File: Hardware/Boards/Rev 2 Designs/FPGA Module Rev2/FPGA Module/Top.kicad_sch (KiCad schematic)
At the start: 6 parts

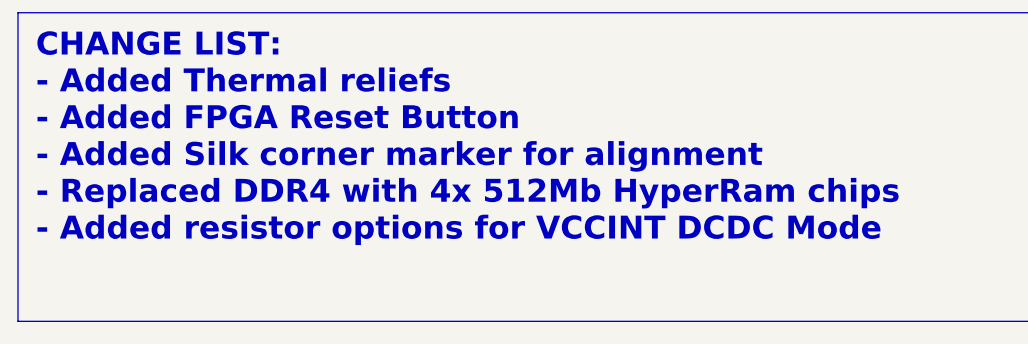
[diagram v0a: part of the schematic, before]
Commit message: Rev 2 IO module complete
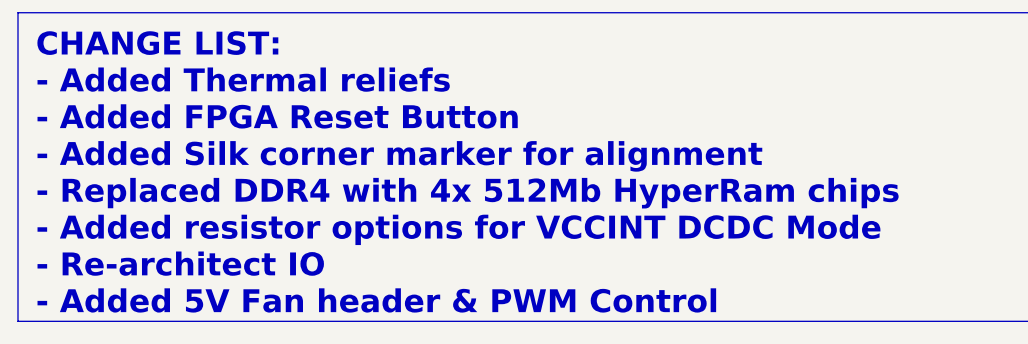
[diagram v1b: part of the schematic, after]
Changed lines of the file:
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@@
 		)
 	)
-	(text_box "CHANGE LIST:\n- Added Thermal reliefs\n- Added FPGA Reset Button\n- Added Silk corner marker for alignment\n- Replaced DDR4 with 4x 512Mb HyperRam chips\n- Added resistor options for VCCINT DCDC Mode\n"
+	(text_box "CHANGE LIST:\n- Added Thermal reliefs\n- Added FPGA Reset Button\n- Added Silk corner marker for alignment\n- Replaced DDR4 with 4x 512Mb HyperRam chips\n- Added resistor options for VCCINT DCDC Mode\n- Re-architect IO\n- Added 5V Fan header & PWM Control\n"
 		(exclude_from_sim no)
 		(at 17.78 247.015 0)

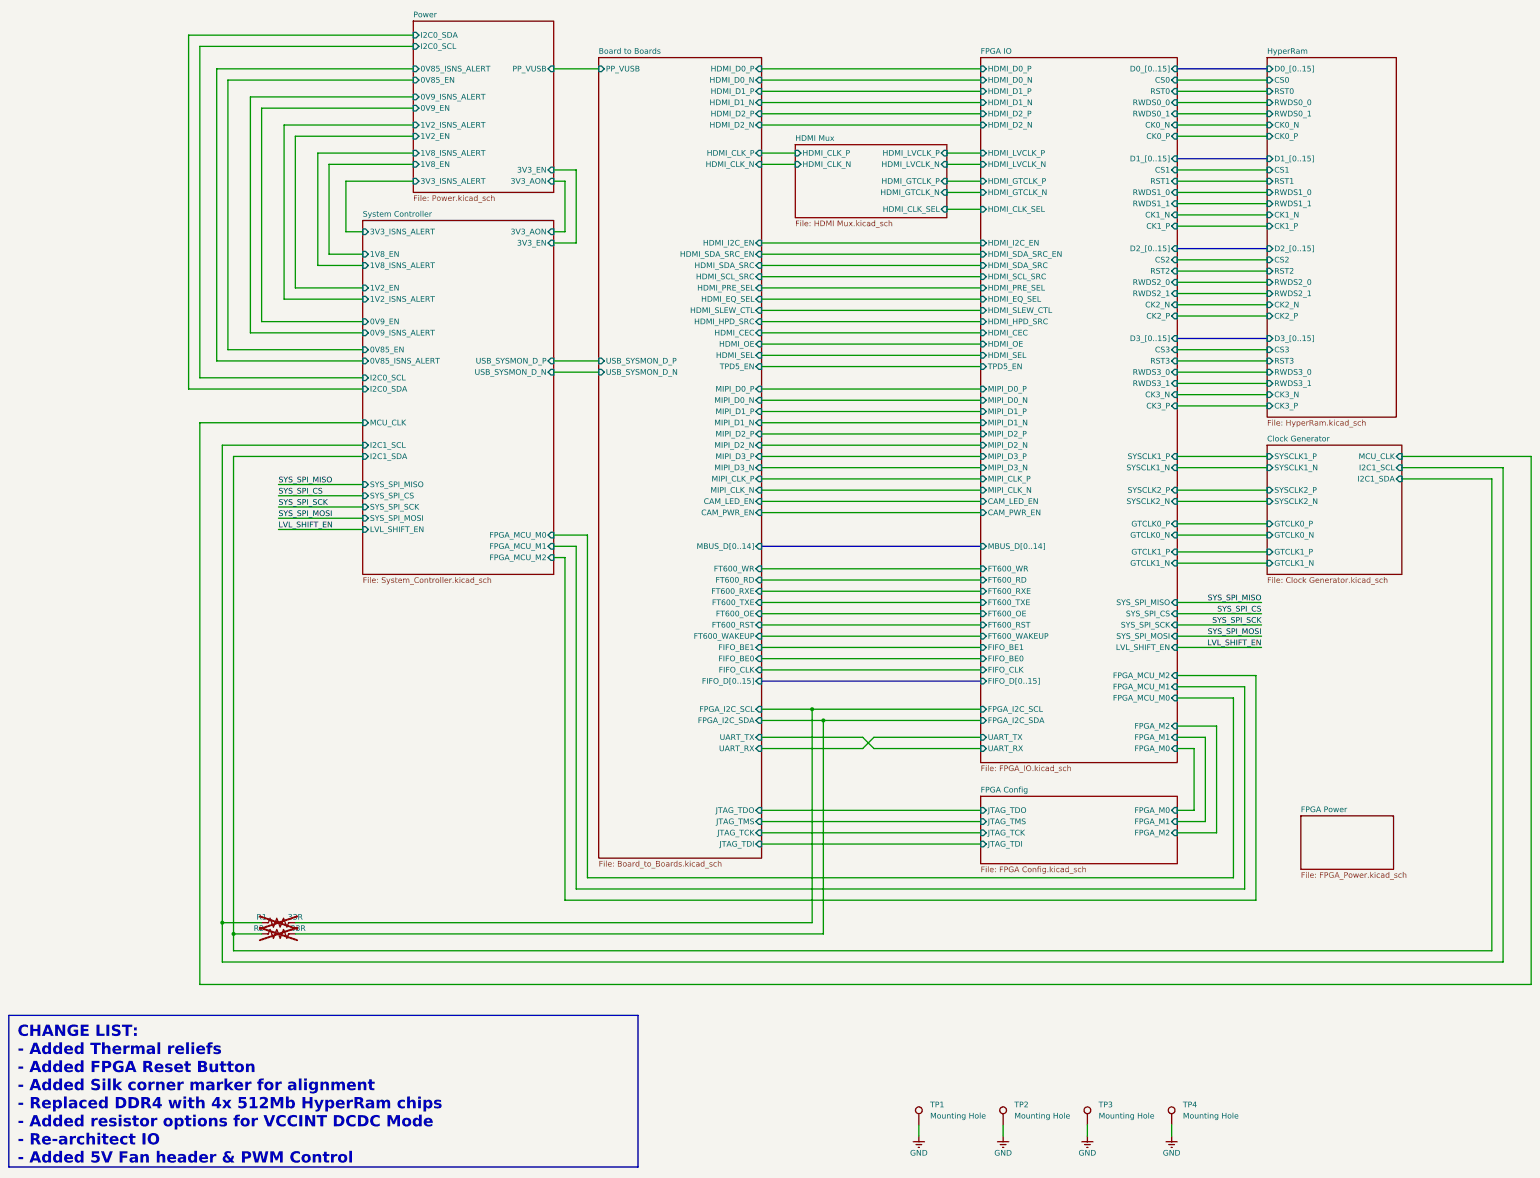
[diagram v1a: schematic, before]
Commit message: FPGA Module Rev 2 Layout Begun
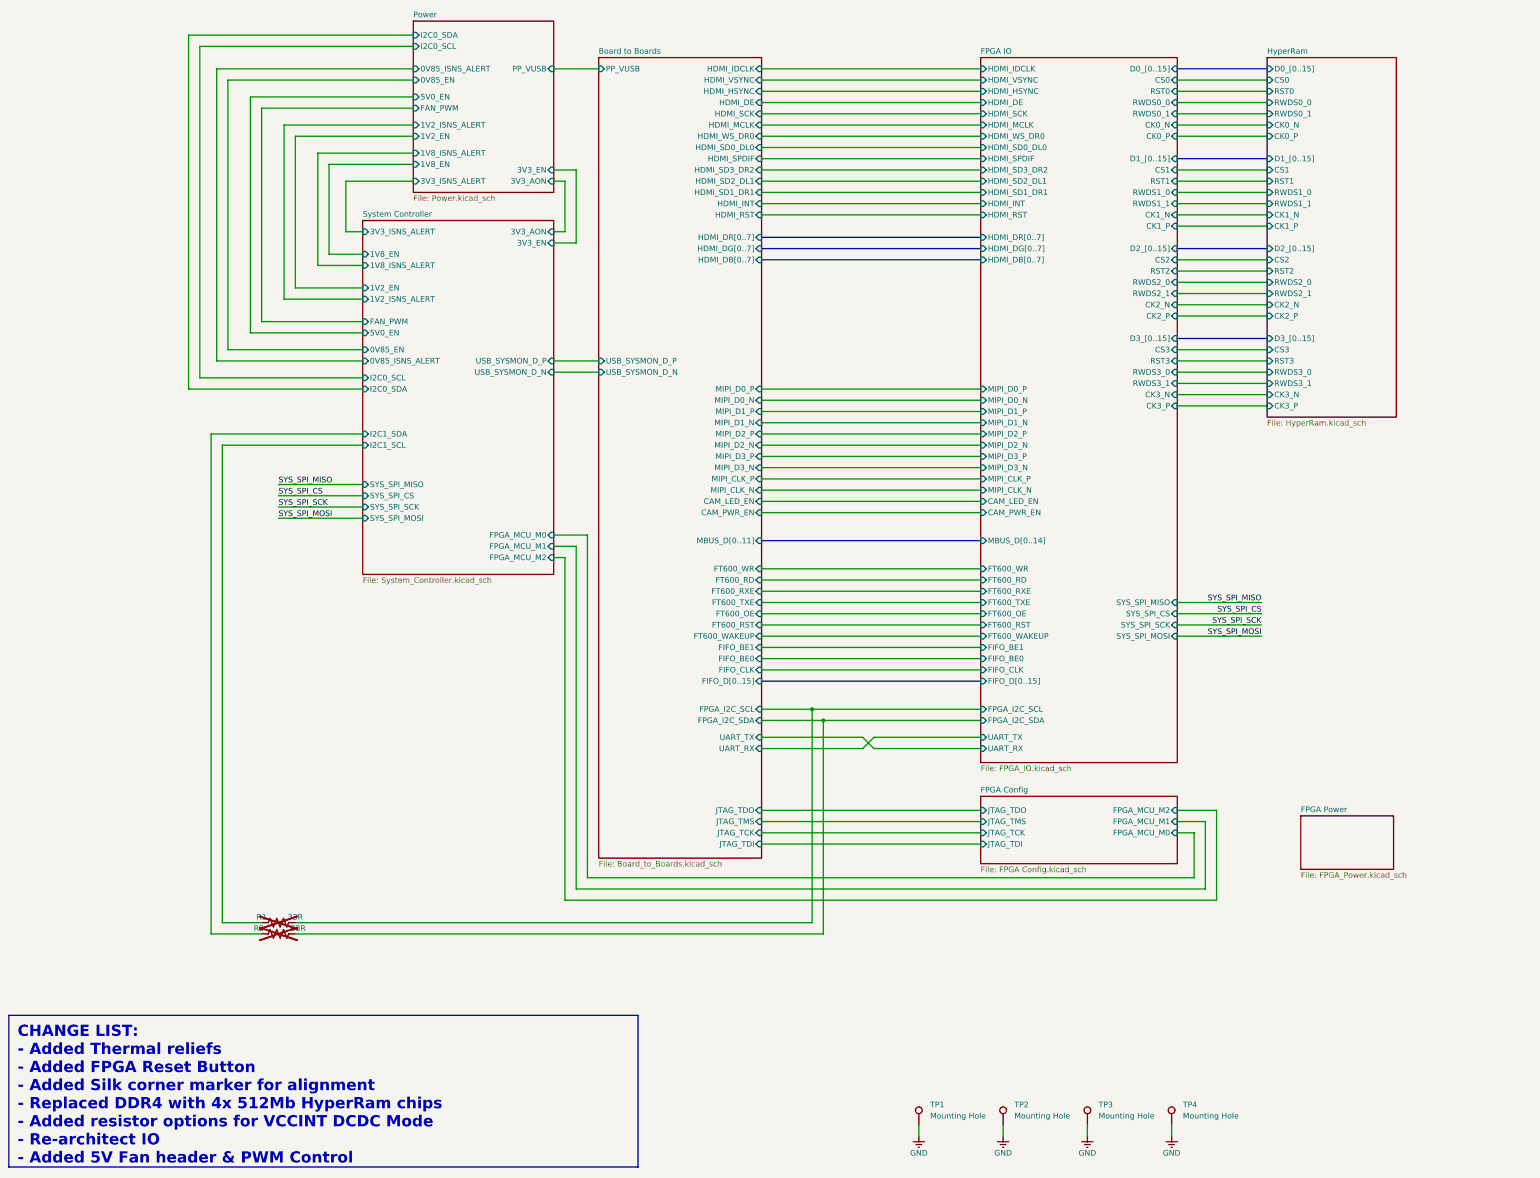
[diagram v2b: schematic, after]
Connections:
- net Clock Generator/I2C1_SCL renamed System Controller/I2C1_SCL
- net Clock Generator/I2C1_SDA renamed System Controller/I2C1_SDA
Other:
- removed sheet Clock Generator
- removed sheet HDMI Mux
- sheet Board to Boards ports: added HDMI_DB[0..7], HDMI_DE, HDMI_DG[0..7], HDMI_DR[0..7], HDMI_HSYNC, HDMI_IDCLK, HDMI_INT, HDMI_MCLK, HDMI_RST, HDMI_SCK, HDMI_SD0_DL0, HDMI_SD1_DR1, HDMI_SD2_DL1, HDMI_SD3_DR2, HDMI_SPDIF, HDMI_VSYNC, HDMI_WS_DR0, MBUS_D[0..11]; removed HDMI_CEC, HDMI_CLK_N, HDMI_CLK_P, HDMI_D0_N, HDMI_D0_P, HDMI_D1_N, HDMI_D1_P, HDMI_D2_N, HDMI_D2_P, HDMI_EQ_SEL, HDMI_HPD_SRC, HDMI_I2C_EN, HDMI_OE, HDMI_PRE_SEL, HDMI_SCL_SRC, HDMI_SDA_SRC, HDMI_SDA_SRC_EN, HDMI_SEL, HDMI_SLEW_CTL, MBUS_D[0..14], TPD5_EN
- sheet FPGA Config ports: added FPGA_MCU_M0, FPGA_MCU_M1, FPGA_MCU_M2; removed FPGA_M0, FPGA_M1, FPGA_M2
- sheet FPGA IO ports: added HDMI_DB[0..7], HDMI_DE, HDMI_DG[0..7], HDMI_DR[0..7], HDMI_HSYNC, HDMI_IDCLK, HDMI_INT, HDMI_MCLK, HDMI_RST, HDMI_SCK, HDMI_SD0_DL0, HDMI_SD1_DR1, HDMI_SD2_DL1, HDMI_SD3_DR2, HDMI_SPDIF, HDMI_VSYNC, HDMI_WS_DR0; removed FPGA_M0, FPGA_M1, FPGA_M2, FPGA_MCU_M0, FPGA_MCU_M1, FPGA_MCU_M2, GTCLK0_N, GTCLK0_P, GTCLK1_N, GTCLK1_P, HDMI_CEC, HDMI_CLK_SEL, HDMI_D0_N, HDMI_D0_P, HDMI_D1_N, HDMI_D1_P, HDMI_D2_N, HDMI_D2_P, HDMI_EQ_SEL, HDMI_GTCLK_N, HDMI_GTCLK_P, HDMI_HPD_SRC, HDMI_I2C_EN, HDMI_LVCLK_N, HDMI_LVCLK_P, HDMI_OE, HDMI_PRE_SEL, HDMI_SCL_SRC, HDMI_SDA_SRC, HDMI_SDA_SRC_EN, HDMI_SEL, HDMI_SLEW_CTL, LVL_SHIFT_EN, SYSCLK1_N, SYSCLK1_P, SYSCLK2_N, SYSCLK2_P, TPD5_EN
- sheet Power ports: added 5V0_EN, FAN_PWM; removed 0V9_EN, 0V9_ISNS_ALERT
- sheet System Controller ports: added 5V0_EN, FAN_PWM; removed 0V9_EN, 0V9_ISNS_ALERT, LVL_SHIFT_EN, MCU_CLK

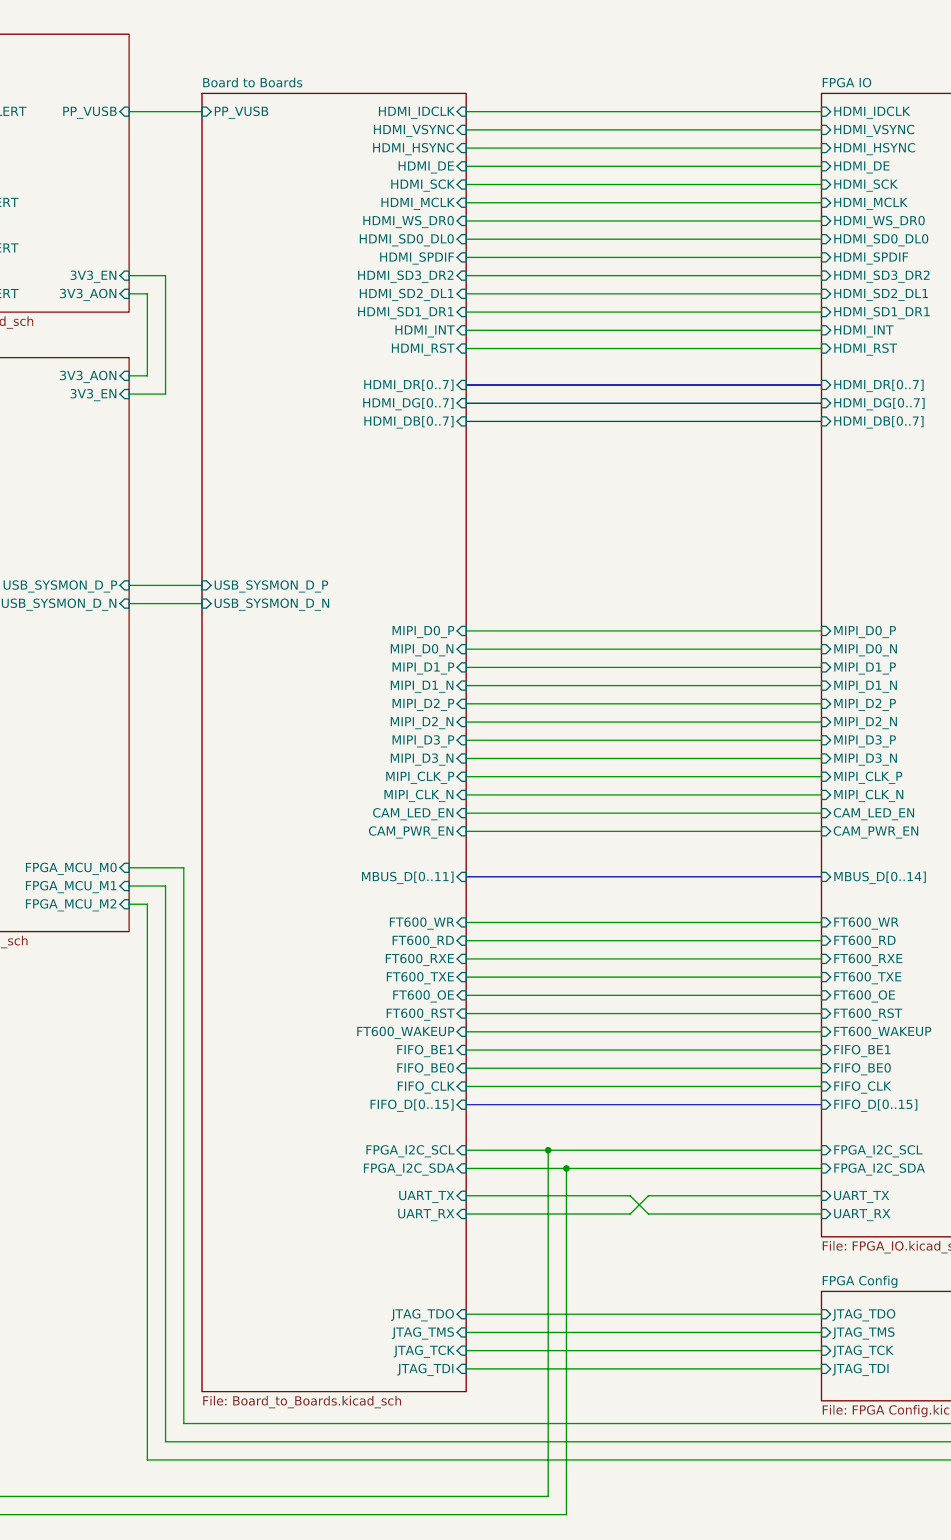
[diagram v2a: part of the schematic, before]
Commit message: Updated Schematics & created pixel combiner HDL
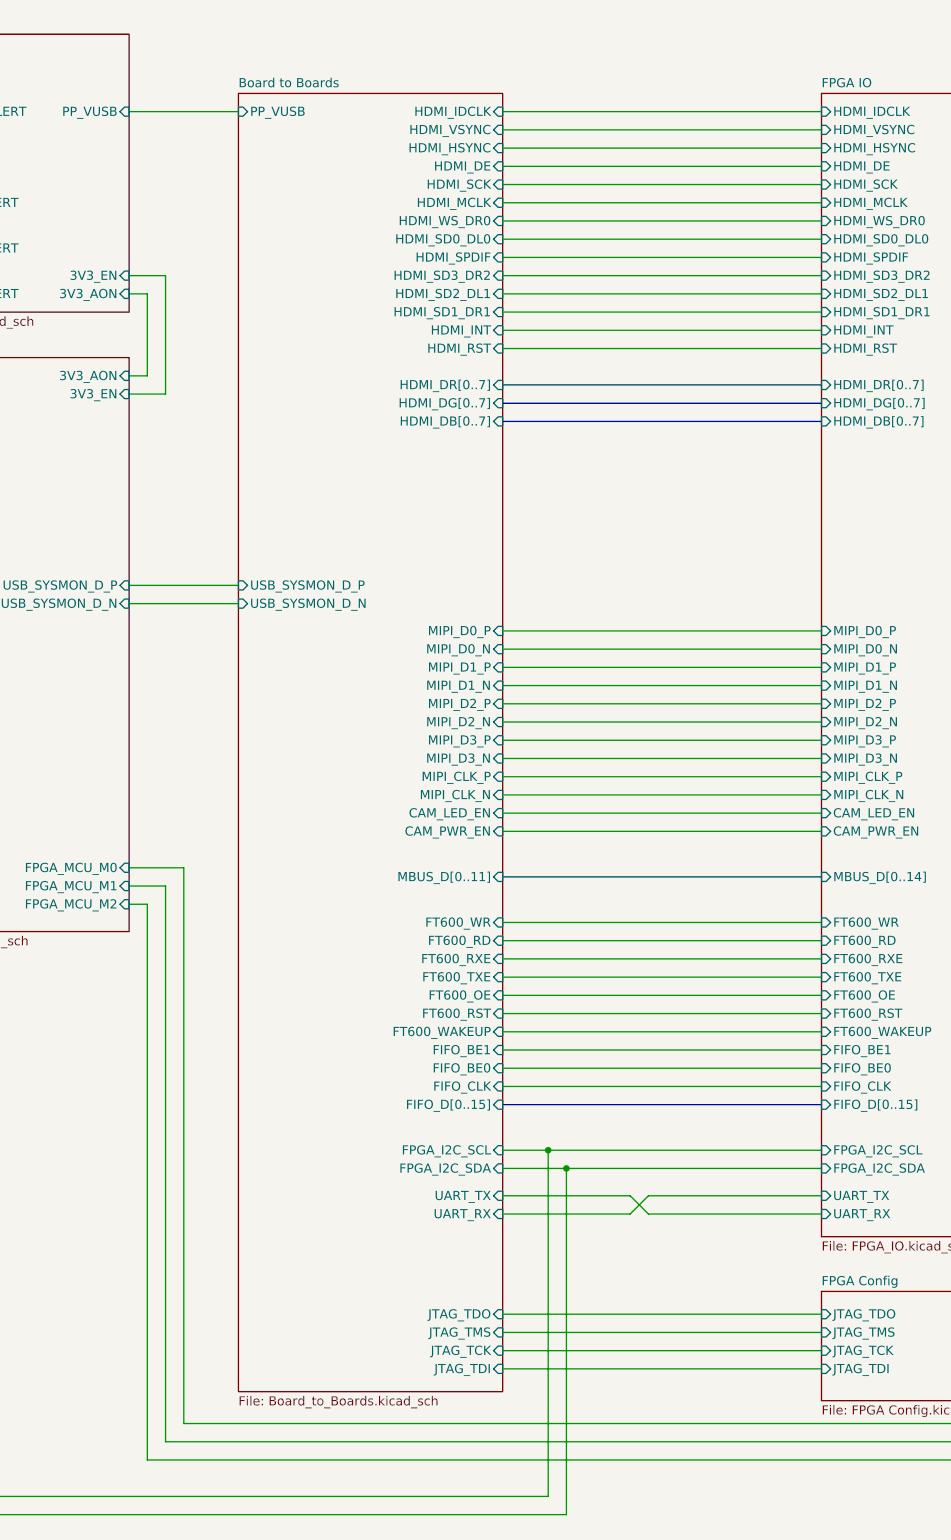
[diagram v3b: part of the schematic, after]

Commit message: Added diagrams, papers and presentations
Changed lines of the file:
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@@
 (kicad_sch
-	(version 20231120)
+	(version 20250114)
 	(generator "eeschema")
-	(generator_version "8.0")
+	(generator_version "9.0")
 	(paper "A3")
 	(title_block
@@
 		(comment 1 "Designed by John Hofmeyr")
 	)
+	(text_box "CHANGE LIST:\n- Added Thermal reliefs\n- Added FPGA Reset Button\n- Added Silk corner marker for alignment\n- Replaced DDR4 with 4x 512Mb HyperRam chips\n- Added resistor options for VCCINT DCDC Mode\n- Re-architect IO\n- Added 5V Fan header & PWM Control\n"
+		(exclude_from_sim no)
+		(at 17.78 247.015 0)
+		(size 142.24 34.29)
+		(margins 1.905 1.905 1.905 1.905)
+		(stroke
+			(width 0)
+			(type default)
+		)
+		(fill
+			(type none)
+		)
+		(effects
+			(font
+				(size 2.54 2.54)
+				(thickness 0.508)
+				(bold yes)
+			)
+			(justify left top)
+		)
+	)
 	(junction
 		(at 201.93 180.34)
@@
 		)
 	)
-	(text_box "CHANGE LIST:\n- Added Thermal reliefs\n- Added FPGA Reset Button\n- Added Silk corner marker for alignment\n- Replaced DDR4 with 4x 512Mb HyperRam chips\n- Added resistor options for VCCINT DCDC Mode\n- Re-architect IO\n- Added 5V Fan header & PWM Control\n"
-		(exclude_from_sim no)
-		(at 17.78 247.015 0)
-		(size 142.24 34.29)
-		(stroke
-			(width 0)
-			(type default)
-		)
-		(fill
-			(type none)
-		)
-		(effects
-			(font
-				(size 2.54 2.54)
-				(thickness 0.508)
-				(bold yes)
-			)
-			(justify left top)
-		)
-	)
 	(label "SYS_SPI_MOSI"
 		(at 78.74 134.62 0)
-		(fields_autoplaced yes)
 		(effects
 			(font
@@
 	(label "SYS_SPI_MISO"
 		(at 78.74 127 0)
-		(fields_autoplaced yes)
 		(effects
 			(font
@@
 	(label "SYS_SPI_MOSI"
 		(at 300.99 161.29 180)
-		(fields_autoplaced yes)
 		(effects
 			(font
@@
 	(label "SYS_SPI_CS"
 		(at 78.74 129.54 0)
-		(fields_autoplaced yes)
 		(effects
 			(font
@@
 	(label "SYS_SPI_SCK"
 		(at 78.74 132.08 0)
-		(fields_autoplaced yes)
 		(effects
 			(font
@@
 	(label "SYS_SPI_MISO"
 		(at 300.99 153.67 180)
-		(fields_autoplaced yes)
 		(effects
 			(font
@@
 	(label "SYS_SPI_CS"
 		(at 300.99 156.21 180)
-		(fields_autoplaced yes)
 		(effects
 			(font
@@
 	(label "SYS_SPI_SCK"
 		(at 300.99 158.75 180)
-		(fields_autoplaced yes)
 		(effects
 			(font
@@
 		(at 237.49 197.485)
 		(size 44.45 15.24)
+		(exclude_from_sim no)
+		(in_bom yes)
+		(on_board yes)
+		(dnp no)
 		(fields_autoplaced yes)
 		(stroke
@@
 		(at 109.22 22.225)
 		(size 31.75 38.735)
+		(exclude_from_sim no)
+		(in_bom yes)
+		(on_board yes)
+		(dnp no)
 		(fields_autoplaced yes)
 		(stroke
@@
 		(at 302.26 30.48)
 		(size 29.21 81.28)
+		(exclude_from_sim no)
+		(in_bom yes)
+		(on_board yes)
+		(dnp no)
 		(fields_autoplaced yes)
 		(stroke
@@
 		(at 237.49 30.48)
 		(size 44.45 159.385)
+		(exclude_from_sim no)
+		(in_bom yes)
+		(on_board yes)
+		(dnp no)
 		(fields_autoplaced yes)
 		(stroke
@@
 		(at 97.79 67.31)
 		(size 43.18 80.01)
+		(exclude_from_sim no)
+		(in_bom yes)
+		(on_board yes)
+		(dnp no)
 		(fields_autoplaced yes)
 		(stroke
@@
 		(at 156.21 30.48)
 		(size 36.83 180.975)
+		(exclude_from_sim no)
+		(in_bom yes)
+		(on_board yes)
+		(dnp no)
 		(fields_autoplaced yes)
 		(stroke
@@
 		(at 309.88 201.93)
 		(size 20.955 12.065)
+		(exclude_from_sim no)
+		(in_bom yes)
+		(on_board yes)
+		(dnp no)
 		(fields_autoplaced yes)
 		(stroke
